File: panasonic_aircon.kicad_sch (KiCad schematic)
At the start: 24 parts, among them J1 Conn_01x04, Q1 BSS138, Q2 BSS138, SW1 SW_Push, U1 ESP32-WROOM-32, U2 AP2112K-3.3, U3 ESP_Programmer

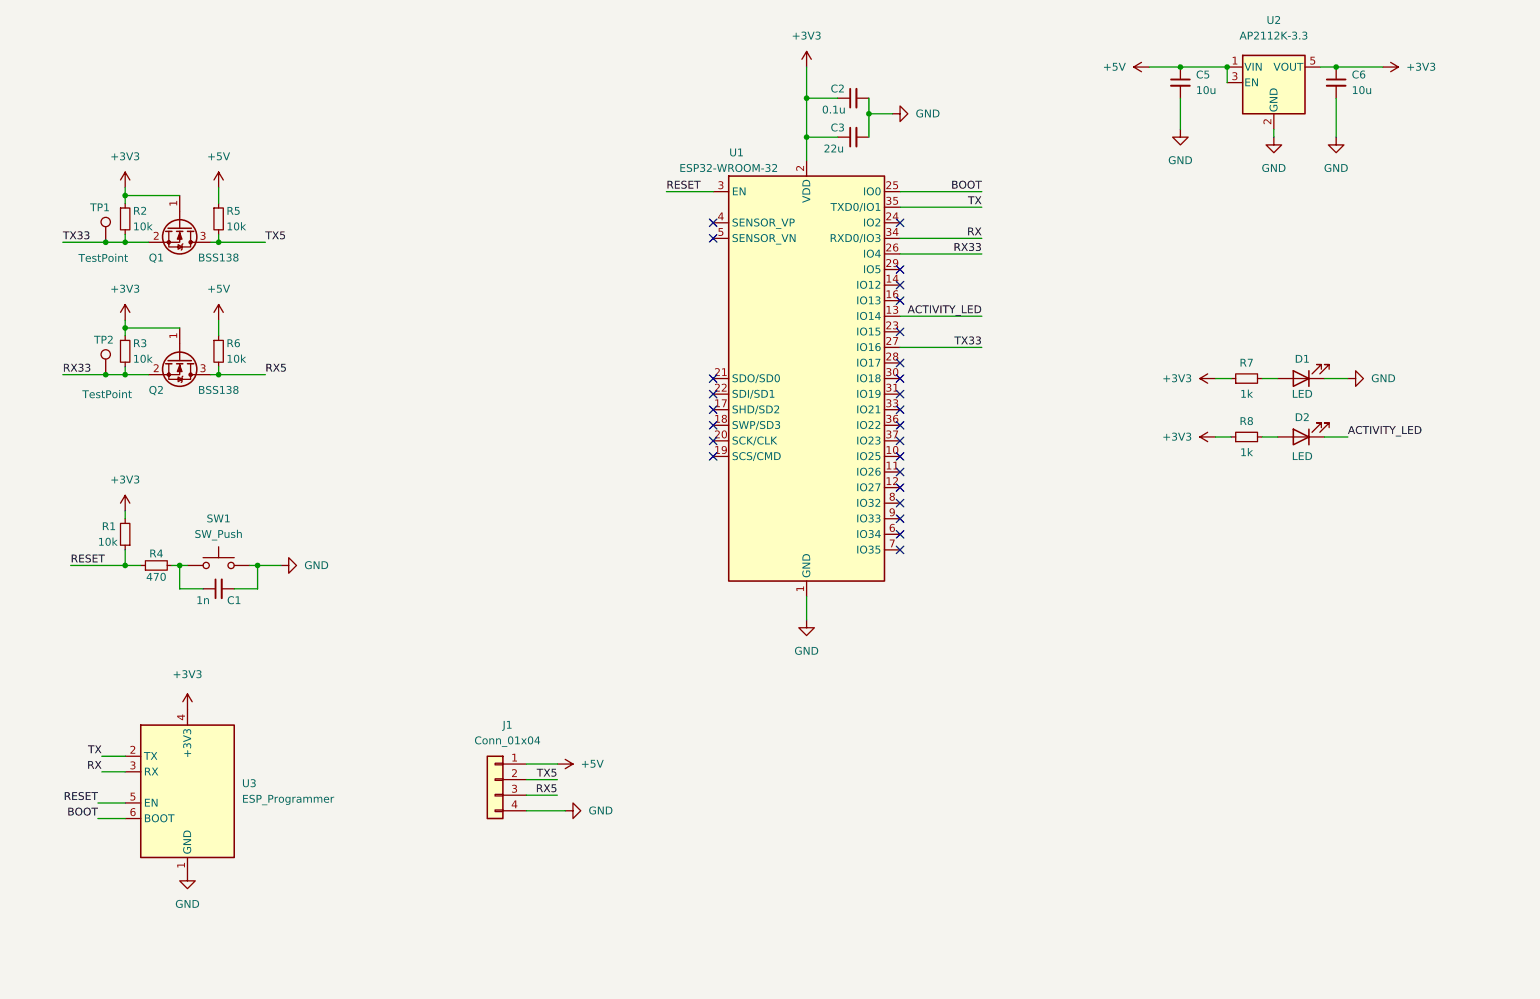
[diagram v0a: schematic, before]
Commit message: Cleanup Schematic layout, label each section
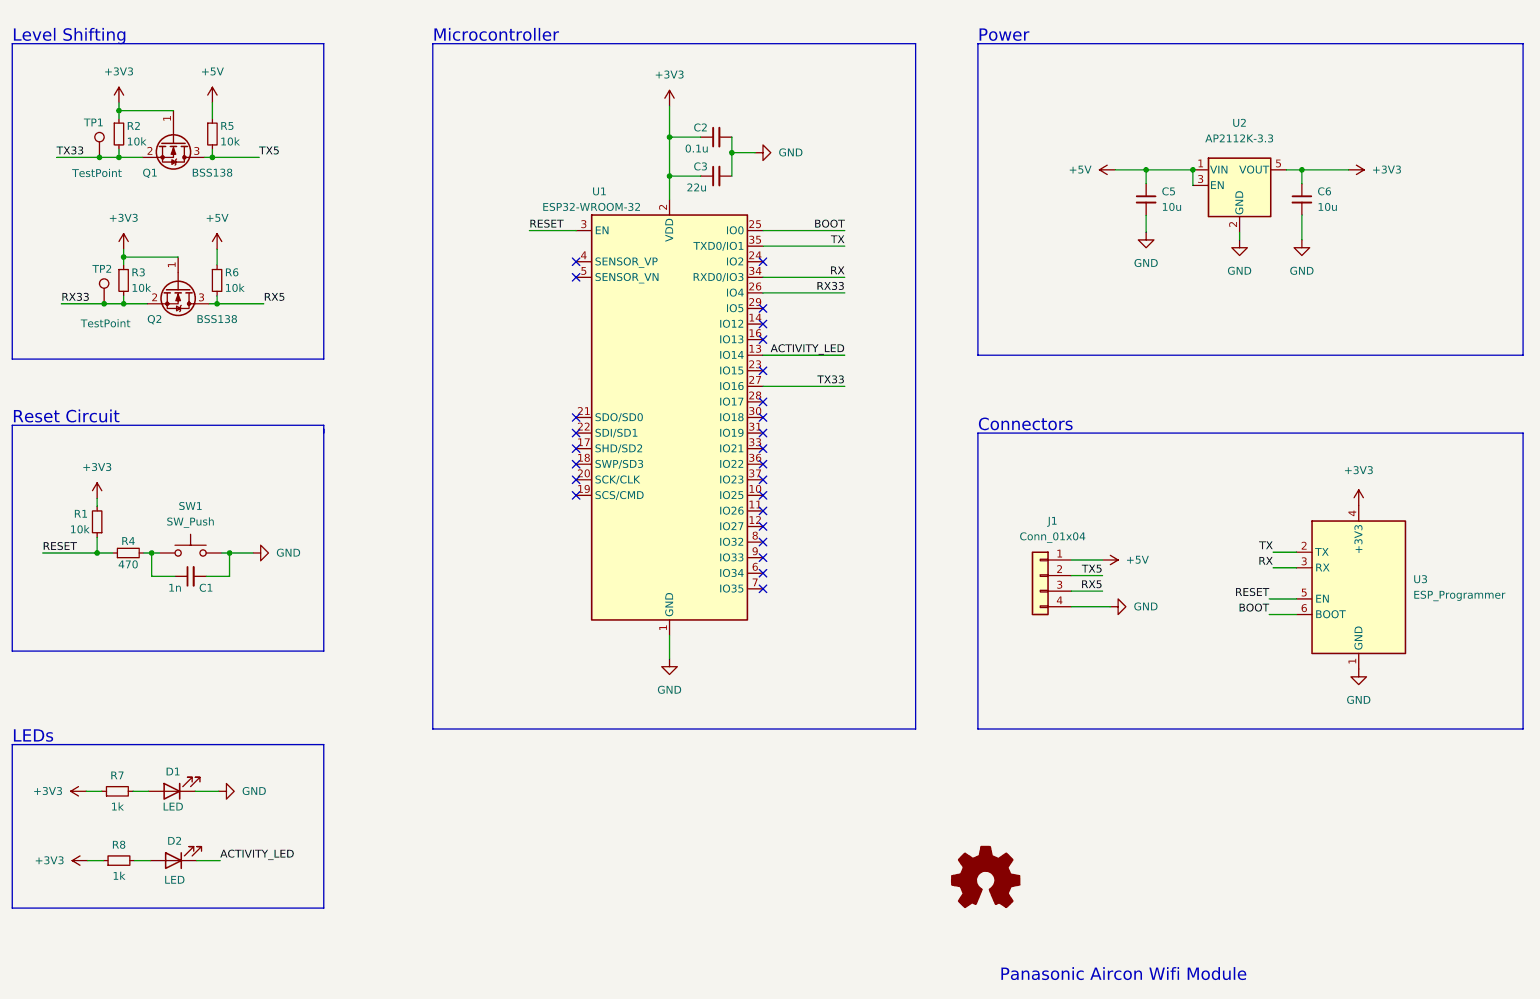
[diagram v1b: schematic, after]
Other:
- note added: "Connectors"
- note added: "LEDs"
- note added: "Level Shifting"
- note added: "Microcontroller"
- note added: "Panasonic Aircon Wifi Module"
- note added: "Power"
- note added: "Reset Circuit"
- moved on the sheet: C1, C2, C3, C5, C6, D1, D2, J1, Q1, Q2, R1, R2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
